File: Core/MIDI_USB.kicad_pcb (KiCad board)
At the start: 4 copper layers, 37.8 x 99.8 mm, 128 parts, among them J1 Conn_01x04, J10 AudioJack3_SwitchTR, J4 Conn_01x06, J5 USB_C_Receptacle_USB2.0, J6 Conn_02x08_Odd_Even, J7 AudioJack3_SwitchTR, J8 AudioJack3_SwitchTR, J9 AudioJack3_SwitchTR, Q1 ZXMP3A13, Q2 PMV88ENER, Q3 MMBT3904, Q5 ZXMP3A13, Q6 MMBT3904, SW1 SW_Push_DPDT, SW2 SW_SPST, SW3 SW_SPST, SW4 SW_SPST, U1 RP2040, U10 MCP2562FD-ESN, U11 CAT250640VI, U12 APS1604M, U13 TPS25820, U2 IS25LP032D, U4 TL072, U5 MIC5504-3.3YM5, U6 ES9023P, U7 PCM1808, U8 TL072, U9 MCP2517FD-xSL, Y1 20MHz, Y2 ECS-120-18-33-JGN-TR3

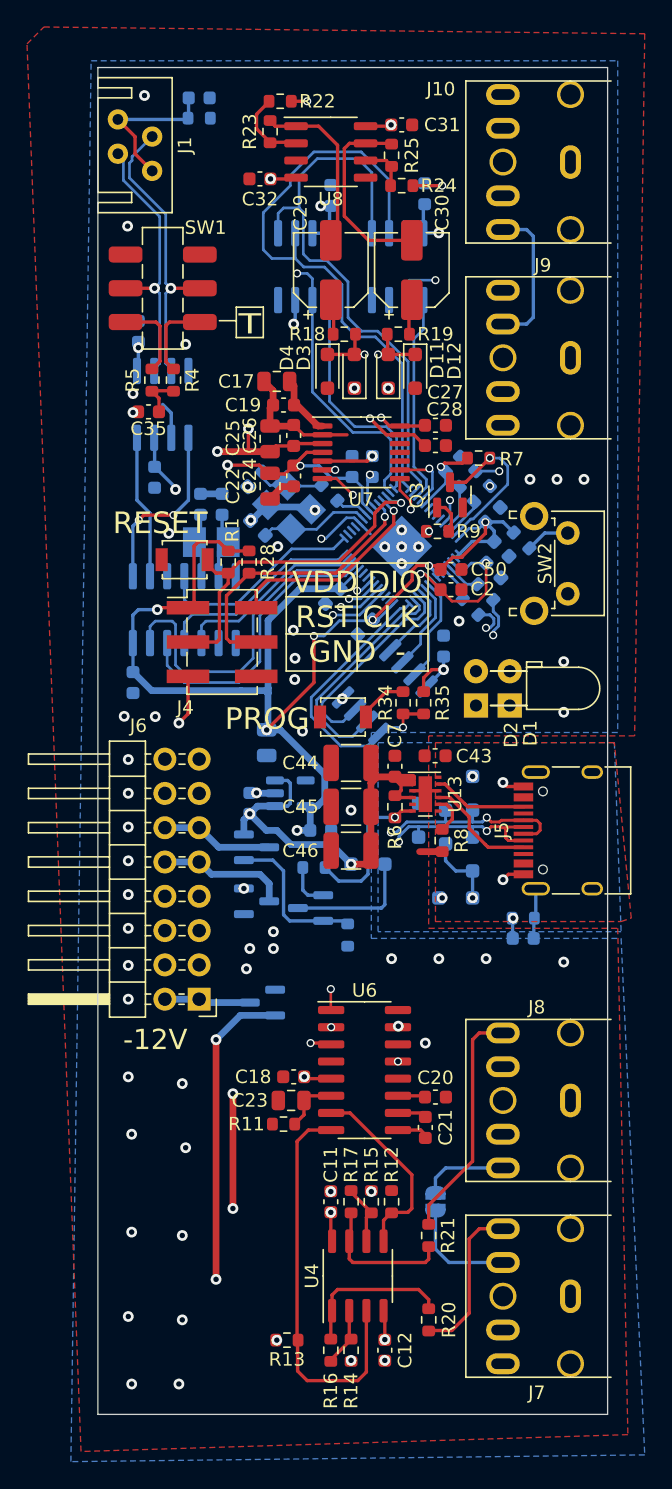
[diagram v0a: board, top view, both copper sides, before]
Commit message: Re-arrange USB components
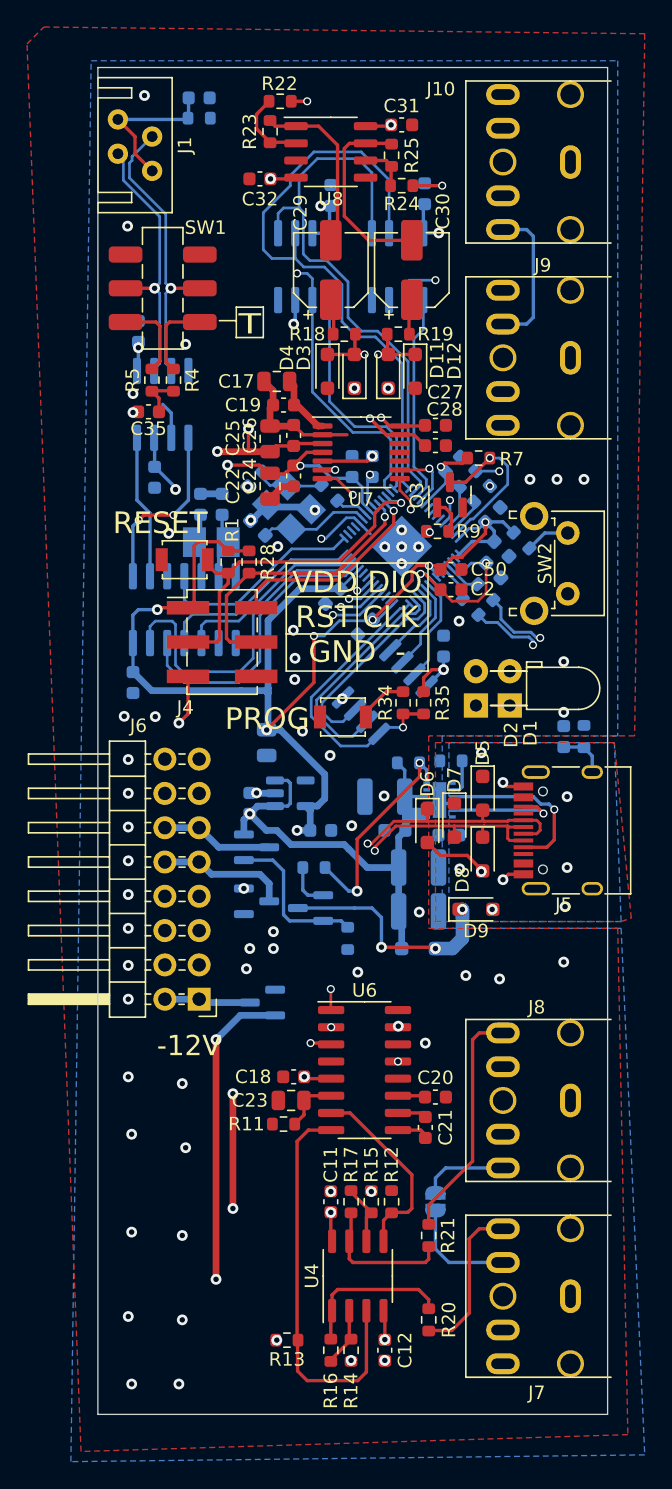
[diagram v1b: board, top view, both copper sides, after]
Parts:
- C43, C44, C45, C46, C7, R6, R8, U13: moved to B.Cu
- D5, D6, D7, D8, D9: moved to F.Cu
- moved C10 15.2 mm to (167.5, 139.8), turned to 90 degrees
- moved R10 14.2 mm to (169.0, 139.8), turned to 90 degrees
- moved C44 9.22 mm to (156.8, 149.5), turned to 0 degrees
- moved C45 9.22 mm to (156.8, 152.8), turned to 0 degrees
- moved D10 7.29 mm to (156.8, 155.5)
- moved C43 5.96 mm to (159.0, 147.1)
- moved R8 5.94 mm to (159.2, 141.6), turned to 180 degrees
- moved C7 4.75 mm to (155.0, 146.8), turned to 180 degrees
- moved C46 4.72 mm to (154.2, 144.2)
- moved R6 3.40 mm to (156.0, 141.8), turned to 0 degrees
- moved D7 2.65 mm to (159.4, 146.0)
- moved D9 1.72 mm to (161.0, 152.6)
- moved D6 1.35 mm to (157.4, 146.4)
- moved U13 1.14 mm to (158.3, 144.5)
- moved D5 0.75 mm to (161.5, 144.0)
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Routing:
- net USB_D+: track 37.2 -> 45.6 mm, vias 3 -> 2
- net USB_D-: track 36.5 -> 44.8 mm, vias 3 -> 2
- net VBUS: track 9.54 -> 17.8 mm, vias 2 -> 8
- net +5V: track 91.8 -> 99.3 mm, vias 7 -> 6
- net Net-(J5-CC1): track 8.34 -> 12.7 mm, vias 0 -> 1
- net GND: track 44.7 -> 41.5 mm, vias 68 -> 70
- net Net-(J5-CC2): track 7.01 -> 8.55 mm, vias 0 -> 1
- net Net-(D6-A): track 31.3 -> 32.5 mm, vias 1 -> 2
- net USB_ID: track 35.8 -> 35.0 mm, vias 2 -> 3
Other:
- rule pad_to_mask_clearance: 0.05 -> 0

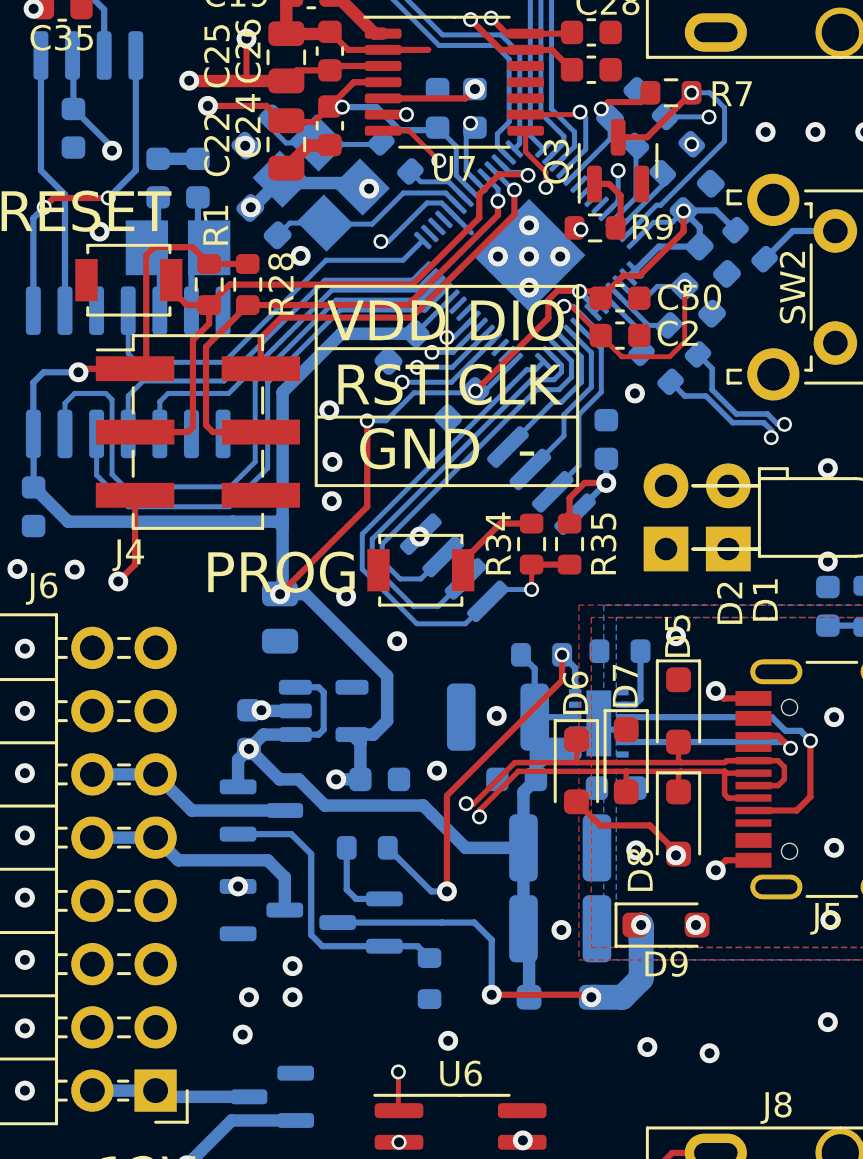
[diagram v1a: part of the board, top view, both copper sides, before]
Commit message: Adjust 5V power protection
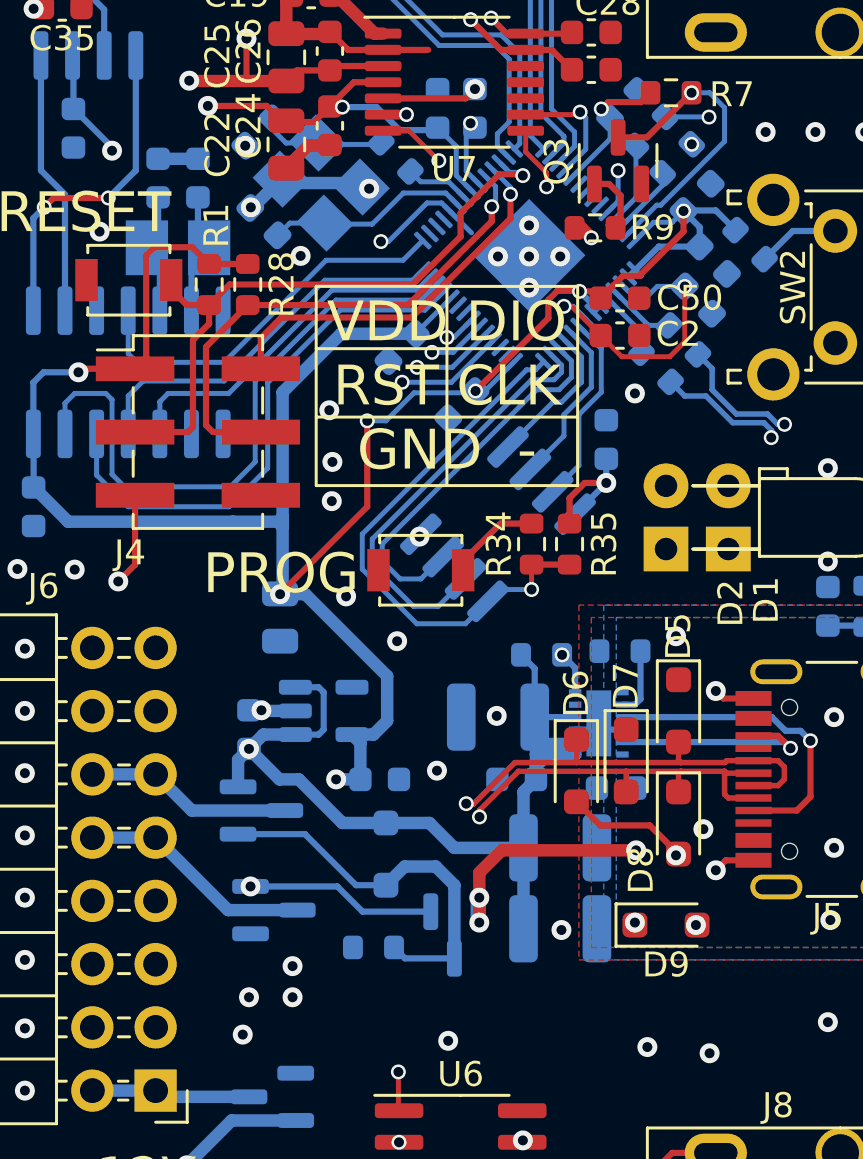
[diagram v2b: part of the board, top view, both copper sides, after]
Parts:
- removed Q6: MMBT3904, Package_TO_SOT_SMD:SOT-23
- removed R30: 100k, Resistor_SMD:R_0603_1608Metric
- added Q4: ZXMP3A13, Package_TO_SOT_SMD:SOT-23, B.Cu at (152.5, 153.0)
- moved D10 9.06 mm to (149.8, 149.8), turned to -90 degrees
- moved R29 2.57 mm to (149.2, 153.5), turned to 180 degrees
- moved Q1 0.50 mm to (145.2, 152.0)
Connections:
- D10 pad 2: VBUS -> Net-(D10-A)
- Q5 pad 1: Net-(Q5-G) -> Net-(D10-A)
- R29 pad 1: Net-(Q5-G) -> Net-(D10-A)
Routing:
- net Net-(D10-A): track 0.00 -> 15.7 mm
- net USB_ID: track 35.0 -> 20.8 mm, vias 3 -> 2
- net Net-(Q5-G): track 11.7 -> 0.00 mm
- net VBUS: track 17.8 -> 8.67 mm, vias 8 -> 9
- net +VDC: track 101.4 -> 109.4 mm
- net Net-(Q6-B): track 3.34 -> 0.00 mm
- net +5V: track 99.3 -> 96.4 mm
- net Net-(U1-VREG_VOUT): track 25.2 -> 26.7 mm

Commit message: Finalize module
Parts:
- C33, C34: value 15pF -> 12pF
- R4, R5: footprint Resistor_SMD:R_0603_1608Metric -> Resistor_SMD:R_0805_2012Metric
- moved R5 0.29 mm to (136.8, 113.2)
- moved R4 0.21 mm to (138.8, 113.2)
